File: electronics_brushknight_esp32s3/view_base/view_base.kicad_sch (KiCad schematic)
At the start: 251 parts, among them J1 BLDC, J2 USB_C_Receptacle_USB2.0, J3 LCD, J4 A, J5 B, J6 LCD - FPC, J7 Conn_01x04_Socket, J8 Conn_01x04_Socket, J9 Conn_01x04_Socket, Q1 MMBT4403, Q4 BSS138, Q5 BSS138, SW1 RST, SW2 Boot, U1 MT6701-CT, U10 ESP32-S3-WROOM-1-N8R8, U2 USBLC6-2SC6, U4 HX711, U5 TMC6300, U7 SN74LV1T34DBV, U7 VL53L0CXV0DH_1, U8 LP5907MFX-2.8, U8 VEML7700, U9 TS1117BCW33_RPG

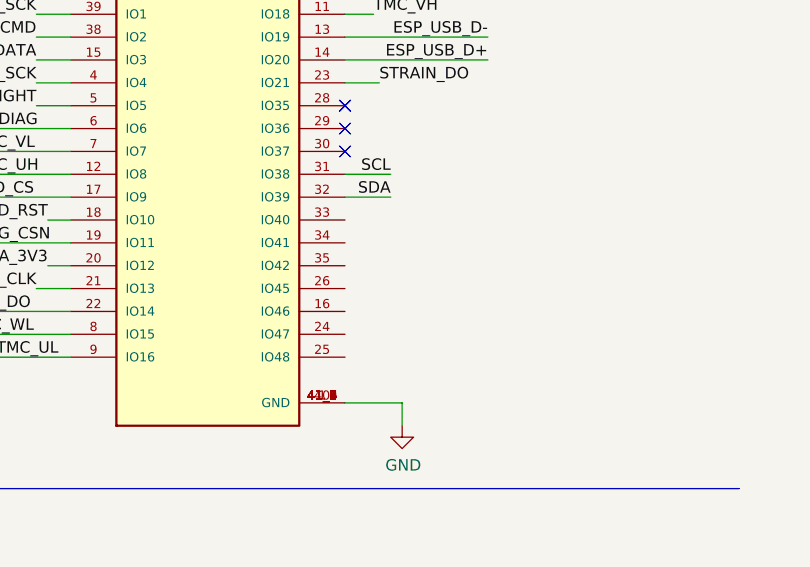
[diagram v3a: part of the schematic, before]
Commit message: working on a panel, run DRC for base pcb
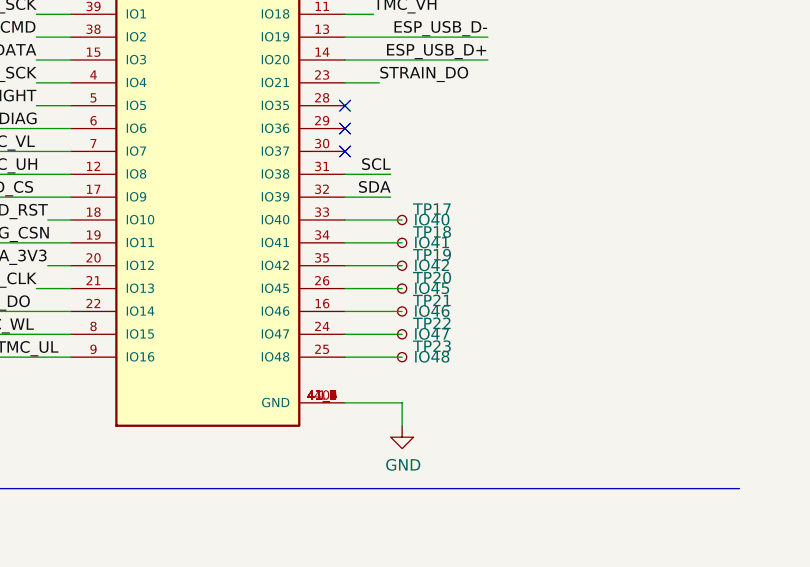
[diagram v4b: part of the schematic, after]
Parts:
- added TP17: IO40, cleaned footprints:TestPoint_Pad_D2.0mm_ValueSilk, symbol Connector:TestPoint_Small
- added TP18: IO41, cleaned footprints:TestPoint_Pad_D2.0mm_ValueSilk, symbol Connector:TestPoint_Small
- added TP19: IO42, cleaned footprints:TestPoint_Pad_D2.0mm_ValueSilk, symbol Connector:TestPoint_Small
- added TP20: IO45, cleaned footprints:TestPoint_Pad_D2.0mm_ValueSilk, symbol Connector:TestPoint_Small
- added TP21: IO46, cleaned footprints:TestPoint_Pad_D2.0mm_ValueSilk, symbol Connector:TestPoint_Small
- added TP22: IO47, cleaned footprints:TestPoint_Pad_D2.0mm_ValueSilk, symbol Connector:TestPoint_Small
- added TP23: IO48, cleaned footprints:TestPoint_Pad_D2.0mm_ValueSilk, symbol Connector:TestPoint_Small
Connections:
- net at U10.16 (IO46): now also TP21.1
- net at U10.24 (IO47): now also TP22.1
- net at U10.25 (IO48): now also TP23.1
- net at U10.26 (IO45): now also TP20.1
- net at U10.33 (IO40): now also TP17.1
- net at U10.34 (IO41): now also TP18.1
- net at U10.35 (IO42): now also TP19.1
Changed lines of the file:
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@@
     (stroke (width 0) (type default))
   )
+  (wire (pts (xy 375.285 69.215) (xy 381.635 69.215))
+    (stroke (width 0) (type default))
+  )
   (wire (pts (xy 114.3 336.55) (xy 114.3 346.71))
     (stroke (width 0) (type default))
@@
     (stroke (width 0) (type default))
   )
+  (wire (pts (xy 375.285 79.375) (xy 381.635 79.375))
+    (stroke (width 0) (type default))
+  )
   (wire (pts (xy 109.22 361.95) (xy 117.475 361.95))
     (stroke (width 0) (type default))
@@
     (stroke (width 0) (type default))
   )
+  (wire (pts (xy 375.285 74.295) (xy 381.635 74.295))
+    (stroke (width 0) (type default))
+  )
   (wire (pts (xy 273.685 431.165) (xy 273.685 441.96))
     (stroke (width 0) (type default))
@@
     (stroke (width 0) (type default))
   )
+  (wire (pts (xy 375.285 76.835) (xy 381.635 76.835))
+    (stroke (width 0) (type default))
+  )
   (wire (pts (xy 334.01 66.675) (xy 344.805 66.675))
     (stroke (width 0) (type default))
@@
     (stroke (width 0) (type default))
   )
+  (wire (pts (xy 375.285 81.915) (xy 381.635 81.915))
+    (stroke (width 0) (type default))
+  )
   (wire (pts (xy 184.785 446.405) (xy 195.58 446.405))
     (stroke (width 0) (type default))
@@
     (stroke (width 0) (type default))
   )
+  (wire (pts (xy 375.285 71.755) (xy 381.635 71.755))
+    (stroke (width 0) (type default))
+  )
   (wire (pts (xy 195.58 204.47) (xy 205.74 204.47))
     (stroke (width 0) (type default))
@@
     (stroke (width 0) (type default))
   )
+  (wire (pts (xy 375.285 84.455) (xy 381.635 84.455))
+    (stroke (width 0) (type default))
+  )
   (wire (pts (xy 90.805 323.215) (xy 101.6 323.215))
     (stroke (width 0) (type default))
@@
     )
   )
+  (symbol (lib_id "Connector:TestPoint_Small") (at 381.635 76.835 0) (unit 1)
+    (in_bom yes) (on_board yes) (dnp no)
+    (property "Reference" "TP20" (at 382.8542 75.6666 0)
+      (effects (font (size 1.27 1.27)) (justify left))
+    )
+    (property "Value" "IO45" (at 382.905 76.835 0)
+      (effects (font (size 1.27 1.27)) (justify left))
+    )
+    (property "Footprint" "cleaned footprints:TestPoint_Pad_D2.0mm_ValueSilk" (at 386.715 76.835 0)
+      (effects (font (size 1.27 1.27)) hide)
+    )
+    (property "Datasheet" "~" (at 386.715 76.835 0)
+      (effects (font (size 1.27 1.27)) hide)
+    )
+    (pin "1")
+    (instances
+      (project "view_base"
+        (path "/5edcefbe-9766-42c8-9529-28d0ec865573"
+          (reference "TP20") (unit 1)
+        )
+      )
+    )
+  )
   (symbol (lib_id "Device:C_Small") (at 255.27 470.535 0) (unit 1)
     (in_bom yes) (on_board yes) (dnp no)
@@
     )
   )
+  (symbol (lib_id "Connector:TestPoint_Small") (at 381.635 74.295 0) (unit 1)
+    (in_bom yes) (on_board yes) (dnp no)
+    (property "Reference" "TP19" (at 382.8542 73.1266 0)
+      (effects (font (size 1.27 1.27)) (justify left))
+    )
+    (property "Value" "IO42" (at 382.905 74.295 0)
+      (effects (font (size 1.27 1.27)) (justify left))
+    )
+    (property "Footprint" "cleaned footprints:TestPoint_Pad_D2.0mm_ValueSilk" (at 386.715 74.295 0)
+      (effects (font (size 1.27 1.27)) hide)
+    )
+    (property "Datasheet" "~" (at 386.715 74.295 0)
+      (effects (font (size 1.27 1.27)) hide)
+    )
+    (pin "1")
+    (instances
+      (project "view_base"
+        (path "/5edcefbe-9766-42c8-9529-28d0ec865573"
+          (reference "TP19") (unit 1)
+        )
+      )
+    )
+  )
+  (symbol (lib_id "Connector:TestPoint_Small") (at 381.635 71.755 0) (unit 1)
+    (in_bom yes) (on_board yes) (dnp no)
+    (property "Reference" "TP18" (at 382.8542 70.5866 0)
+      (effects (font (size 1.27 1.27)) (justify left))
+    )
+    (property "Value" "IO41" (at 382.905 71.755 0)
+      (effects (font (size 1.27 1.27)) (justify left))
+    )
+    (property "Footprint" "cleaned footprints:TestPoint_Pad_D2.0mm_ValueSilk" (at 386.715 71.755 0)
+      (effects (font (size 1.27 1.27)) hide)
+    )
+    (property "Datasheet" "~" (at 386.715 71.755 0)
+      (effects (font (size 1.27 1.27)) hide)
+    )
+    (pin "1")
+    (instances
+      (project "view_base"
+        (path "/5edcefbe-9766-42c8-9529-28d0ec865573"
+          (reference "TP18") (unit 1)
+        )
+      )
+    )
+  )
   (symbol (lib_id "LED:SK6812") (at 101.6 339.09 0) (unit 1)
     (in_bom yes) (on_board yes) (dnp no)
@@
     )
   )
+  (symbol (lib_id "Connector:TestPoint_Small") (at 381.635 69.215 0) (unit 1)
+    (in_bom yes) (on_board yes) (dnp no)
+    (property "Reference" "TP17" (at 382.8542 68.0466 0)
+      (effects (font (size 1.27 1.27)) (justify left))
+    )
+    (property "Value" "IO40" (at 382.905 69.215 0)
+      (effects (font (size 1.27 1.27)) (justify left))
+    )
+    (property "Footprint" "cleaned footprints:TestPoint_Pad_D2.0mm_ValueSilk" (at 386.715 69.215 0)
+      (effects (font (size 1.27 1.27)) hide)
+    )
+    (property "Datasheet" "~" (at 386.715 69.215 0)
+      (effects (font (size 1.27 1.27)) hide)
+    )
+    (pin "1")
+    (instances
+      (project "view_base"
+        (path "/5edcefbe-9766-42c8-9529-28d0ec865573"
+          (reference "TP17") (unit 1)
+        )
+      )
+    )
+  )
   (symbol (lib_id "LED:SK6812") (at 195.58 339.09 0) (unit 1)
     (in_bom yes) (on_board yes) (dnp no)
@@
     )
   )
+  (symbol (lib_id "Connector:TestPoint_Small") (at 381.635 84.455 0) (unit 1)
+    (in_bom yes) (on_board yes) (dnp no)
+    (property "Reference" "TP23" (at 382.8542 83.2866 0)
+      (effects (font (size 1.27 1.27)) (justify left))
+    )
+    (property "Value" "IO48" (at 382.905 84.455 0)
+      (effects (font (size 1.27 1.27)) (justify left))
+    )
+    (property "Footprint" "cleaned footprints:TestPoint_Pad_D2.0mm_ValueSilk" (at 386.715 84.455 0)
+      (effects (font (size 1.27 1.27)) hide)
+    )
+    (property "Datasheet" "~" (at 386.715 84.455 0)
+      (effects (font (size 1.27 1.27)) hide)
+    )
+    (pin "1")
+    (instances
+      (project "view_base"
+        (path "/5edcefbe-9766-42c8-9529-28d0ec865573"
+          (reference "TP23") (unit 1)
+        )
+      )
+    )
+  )
   (symbol (lib_id "Device:R_Small") (at 441.96 382.905 0) (mirror x) (unit 1)
     (in_bom yes) (on_board yes) (dnp no)
@@
     )
   )
+  (symbol (lib_id "Connector:TestPoint_Small") (at 381.635 81.915 0) (unit 1)
+    (in_bom yes) (on_board yes) (dnp no)
+    (property "Reference" "TP22" (at 382.8542 80.7466 0)
+      (effects (font (size 1.27 1.27)) (justify left))
+    )
+    (property "Value" "IO47" (at 382.905 81.915 0)
+      (effects (font (size 1.27 1.27)) (justify left))
+    )
+    (property "Footprint" "cleaned footprints:TestPoint_Pad_D2.0mm_ValueSilk" (at 386.715 81.915 0)
+      (effects (font (size 1.27 1.27)) hide)
+    )
+    (property "Datasheet" "~" (at 386.715 81.915 0)
+      (effects (font (size 1.27 1.27)) hide)
+    )
+    (pin "1")
+    (instances
+      (project "view_base"
+        (path "/5edcefbe-9766-42c8-9529-28d0ec865573"
+          (reference "TP22") (unit 1)
+        )
+      )
+    )
+  )
   (symbol (lib_id "Device:C_Small") (at 114.3 426.085 0) (unit 1)
     (in_bom yes) (on_board yes) (dnp no)
@@
         )
       )
+    )
+  )
+  (symbol (lib_id "Connector:TestPoint_Small") (at 381.635 79.375 0) (unit 1)
+    (in_bom yes) (on_board yes) (dnp no)
+    (property "Reference" "TP21" (at 382.8542 78.2066 0)
+      (effects (font (size 1.27 1.27)) (justify left))
+    )
+    (property "Value" "IO46" (at 382.905 79.375 0)
+      (effects (font (size 1.27 1.27)) (justify left))
+    )
+    (property "Footprint" "cleaned footprints:TestPoint_Pad_D2.0mm_ValueSilk" (at 386.715 79.375 0)
+      (effects (font (size 1.27 1.27)) hide)
+    )
+    (property "Datasheet" "~" (at 386.715 79.375 0)
+      (effects (font (size 1.27 1.27)) hide)
+    )
+    (pin "1")
+    (instances
+      (project "view_base"
+        (path "/5edcefbe-9766-42c8-9529-28d0ec865573"
+          (reference "TP21") (unit 1)
+        )
+      )

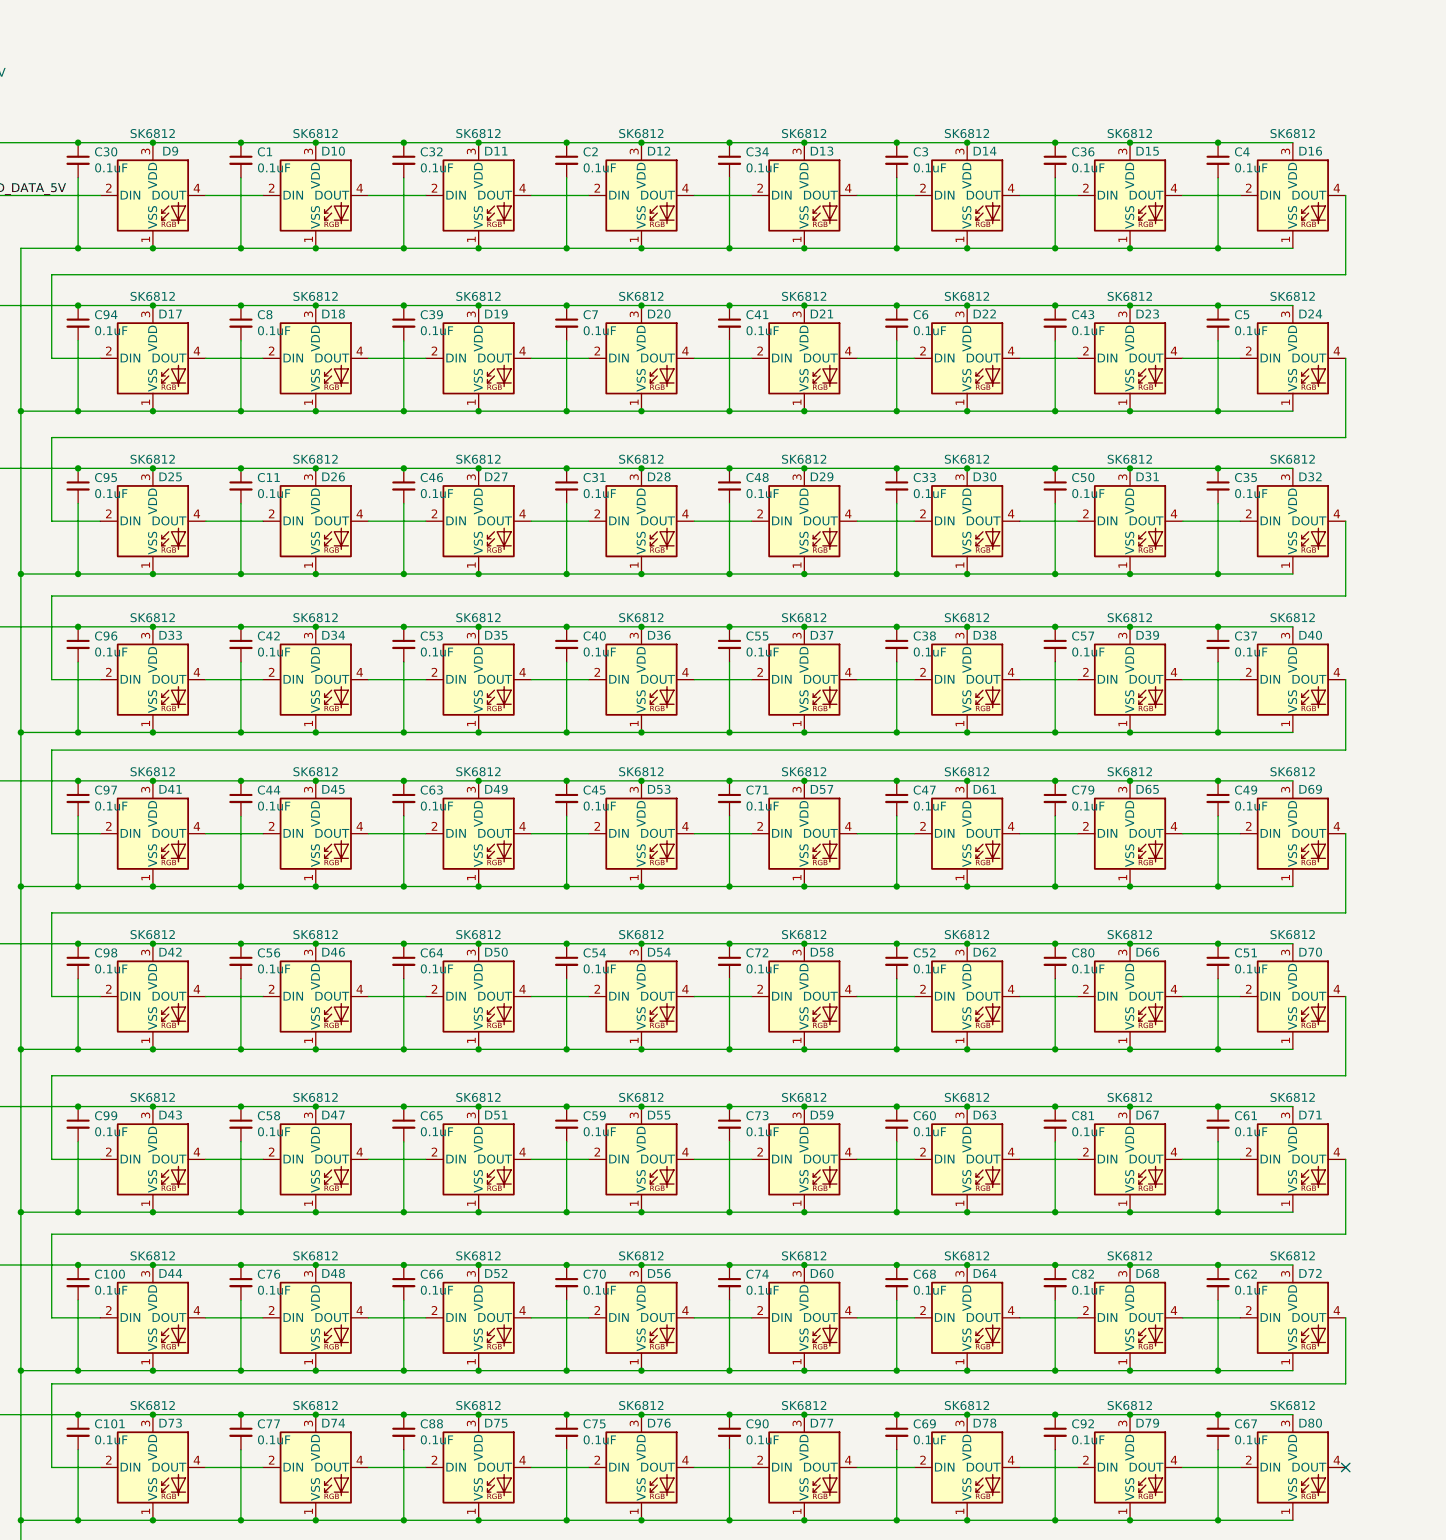
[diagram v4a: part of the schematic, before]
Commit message: Updated ibom for base pcb
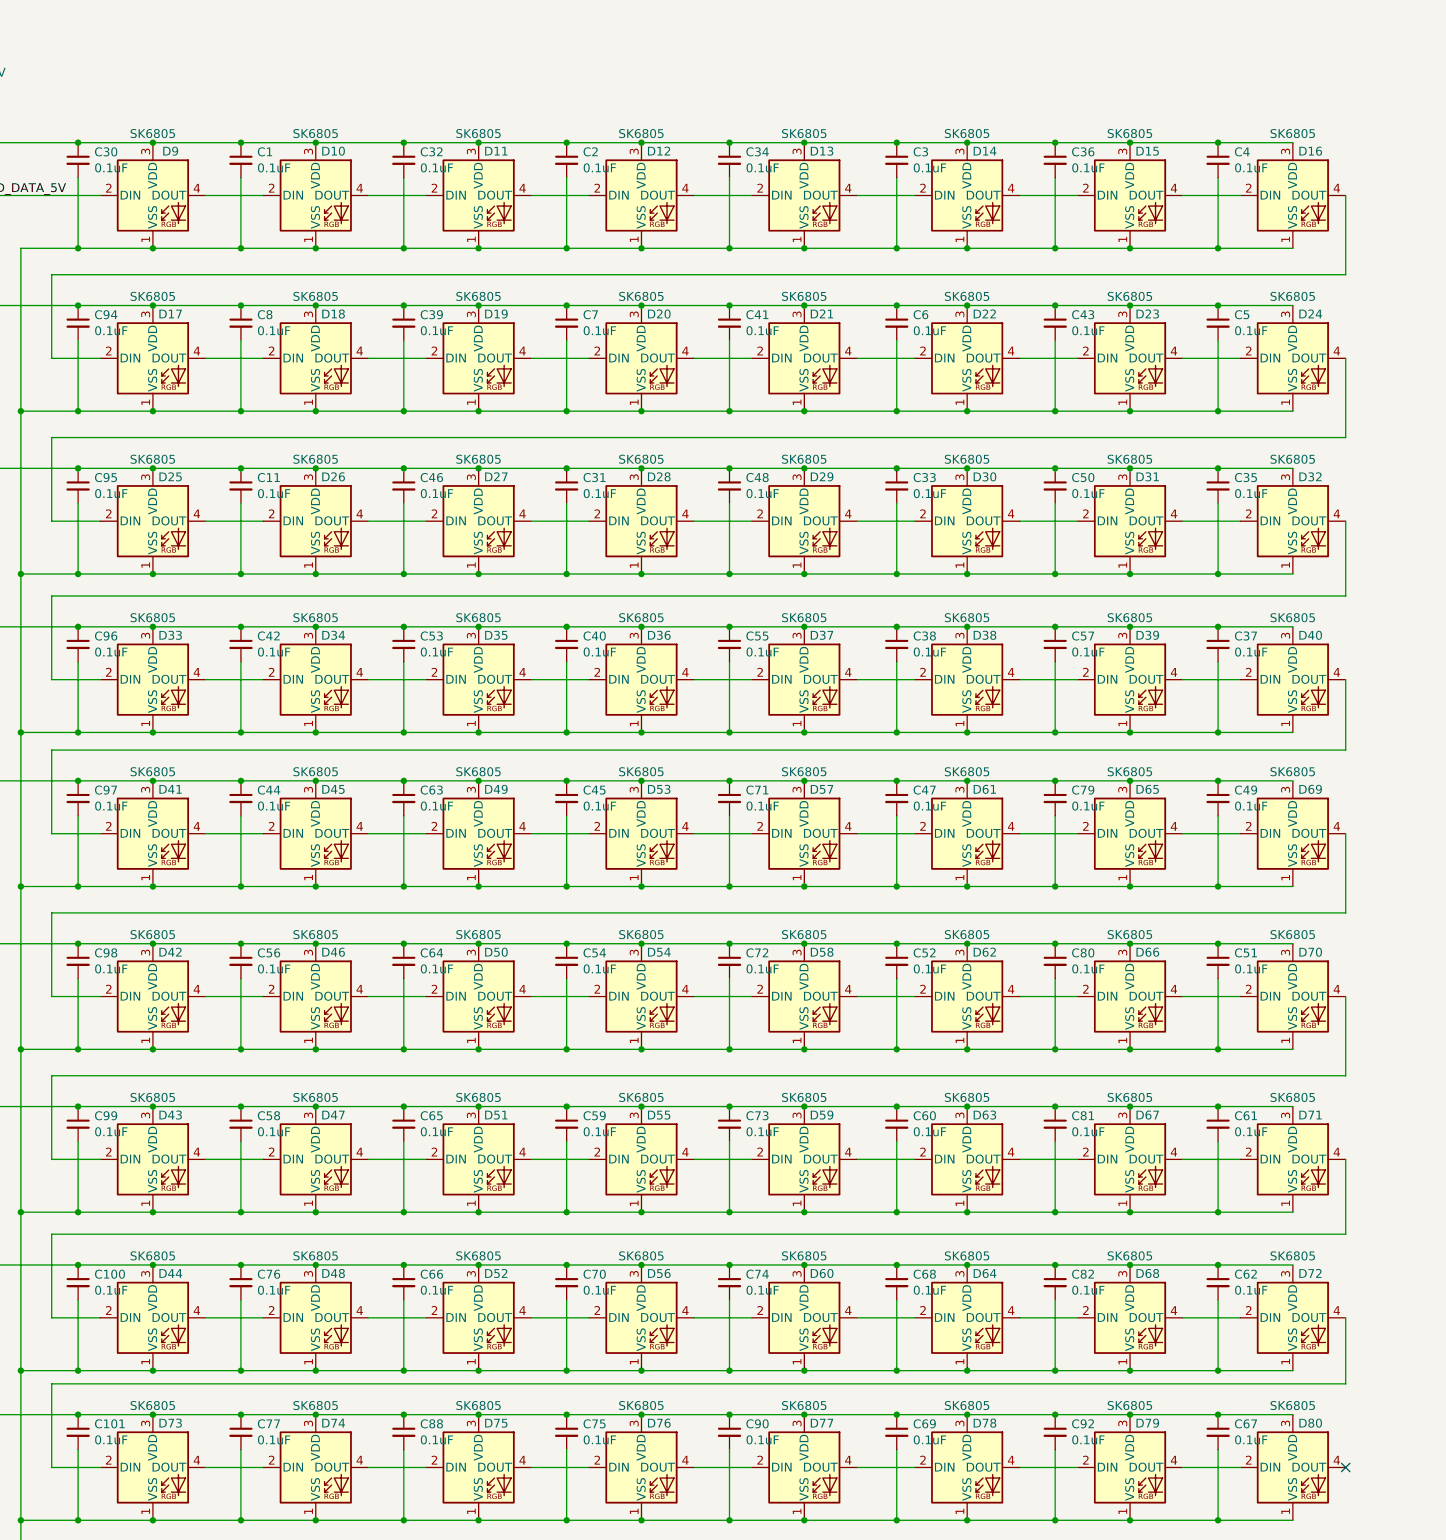
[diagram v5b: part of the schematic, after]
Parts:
- C1, C100, C101, C11, C2, C29, C3, C30, C31, C32, C33, C34, C35, C36, C37, C38, C39, C4, C40, C41, C42, C43, C44, C45, C46, C47, C48, C49, C5, C50, C51, C52, C53, C54, C55, C56, C57, C58, C59, C6, C60, C61, C62, C63, C64, C65, C66, C67, C68, C69, C7, C70, C71, C72, C73, C74, C75, C76, C77, C79, C8, C80, C81, C82, C88, C90, C92, C94, C95, C96, C97, C98, C99: Digikey 1276-1935-1-ND -> (none); LCSC C1591 -> C83056; Mouser 187-CL10B104KB8NNWC -> (none)
- C27, C38: LCSC (none) -> C38898
- C39: LCSC (none) -> C1591
- D10, D11, D12, D13, D14, D15, D16, D17, D18, D19, D20, D21, D22, D23, D24, D25, D26, D27, D28, D29, D30, D31, D32, D33, D34, D35, D36, D37, D38, D39, D40, D41, D42, D43, D44, D45, D46, D47, D48, D49, D50, D51, D52, D53, D54, D55, D56, D57, D58, D59, D60, D61, D62, D63, D64, D65, D66, D67, D68, D69, D70, D71, D72, D73, D74, D75, D76, D77, D78, D79, D80, D9: value SK6812 -> SK6805; AliExpress (none) -> https://es.aliexpress.com/item/32957257689.html
- J6: Mouser (none) -> 649-59453081110EDHLF
- J7, J8, J9: Mouser (none) -> 485-4208
- Q4, Q5: LCSC (none) -> C2874697
- SW1, SW2: LCSC (none) -> C116501
- U2: LCSC (none) -> C7519
- U7: Mouser (none) -> 511-VL53L0CXV0DH/1
- U8: Mouser (none) -> 595-LP5907MFX-2.8NPB
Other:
- company: Scott Bezek -> Scott Bezek | Grigorii Merkushev (brushknight)
